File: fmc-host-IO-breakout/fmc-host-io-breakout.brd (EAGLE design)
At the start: 135 x 195 mm, 79 parts, among them J4 12226-8250-00FR, X1 1503_02

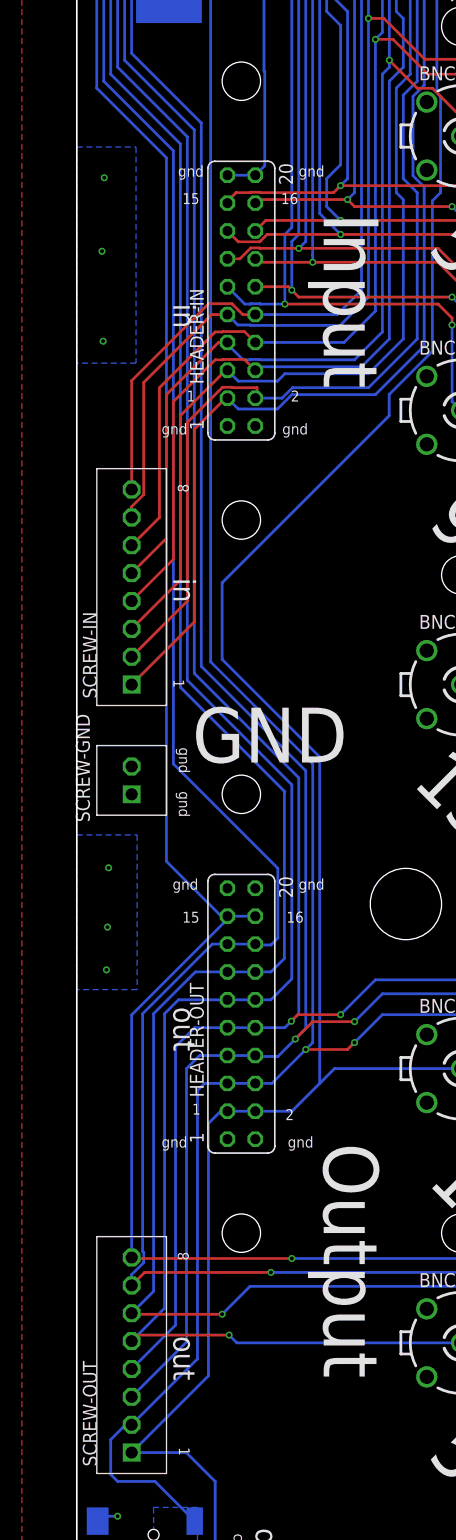
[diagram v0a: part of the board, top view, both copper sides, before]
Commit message: Made analog io board compatible with screwless screw terminals
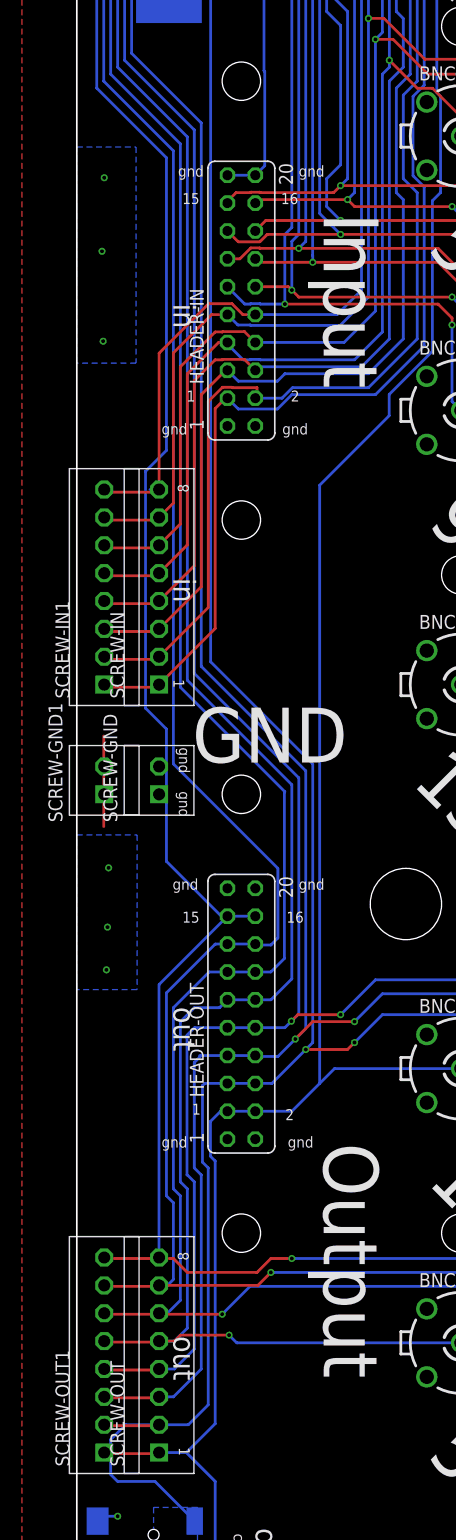
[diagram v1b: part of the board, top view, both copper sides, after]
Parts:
- added SCREW-GND1: SCREW2, jonnew:SCREW2
- added SCREW-IN1, SCREW-OUT1: SCREW8, jonnew:SCREW8
- moved SCREW-GND 2.50 mm to (-37.5, -25.0)
- moved SCREW-IN 2.50 mm to (-37.5, -15.0)
- moved SCREW-OUT 2.50 mm to (-37.5, -85.0)
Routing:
- net AOUT0: track 244.6 -> 233.1 mm
- net AGND: track 229.1 -> 237.3 mm
- net S$9: track 0.00 -> 5.08 mm
- net S$8: track 0.00 -> 5.08 mm
- net S$7: track 0.00 -> 5.08 mm
- net S$6: track 0.00 -> 5.08 mm
- net S$5: track 0.00 -> 5.08 mm
- net S$4: track 0.00 -> 5.08 mm
- net S$3: track 0.00 -> 5.08 mm
- net S$2: track 0.00 -> 5.08 mm
- net S$16: track 0.00 -> 5.08 mm
- net S$15: track 0.00 -> 5.08 mm
- net S$14: track 0.00 -> 5.08 mm
- net S$13: track 0.00 -> 5.08 mm
- net S$12: track 0.00 -> 5.08 mm
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
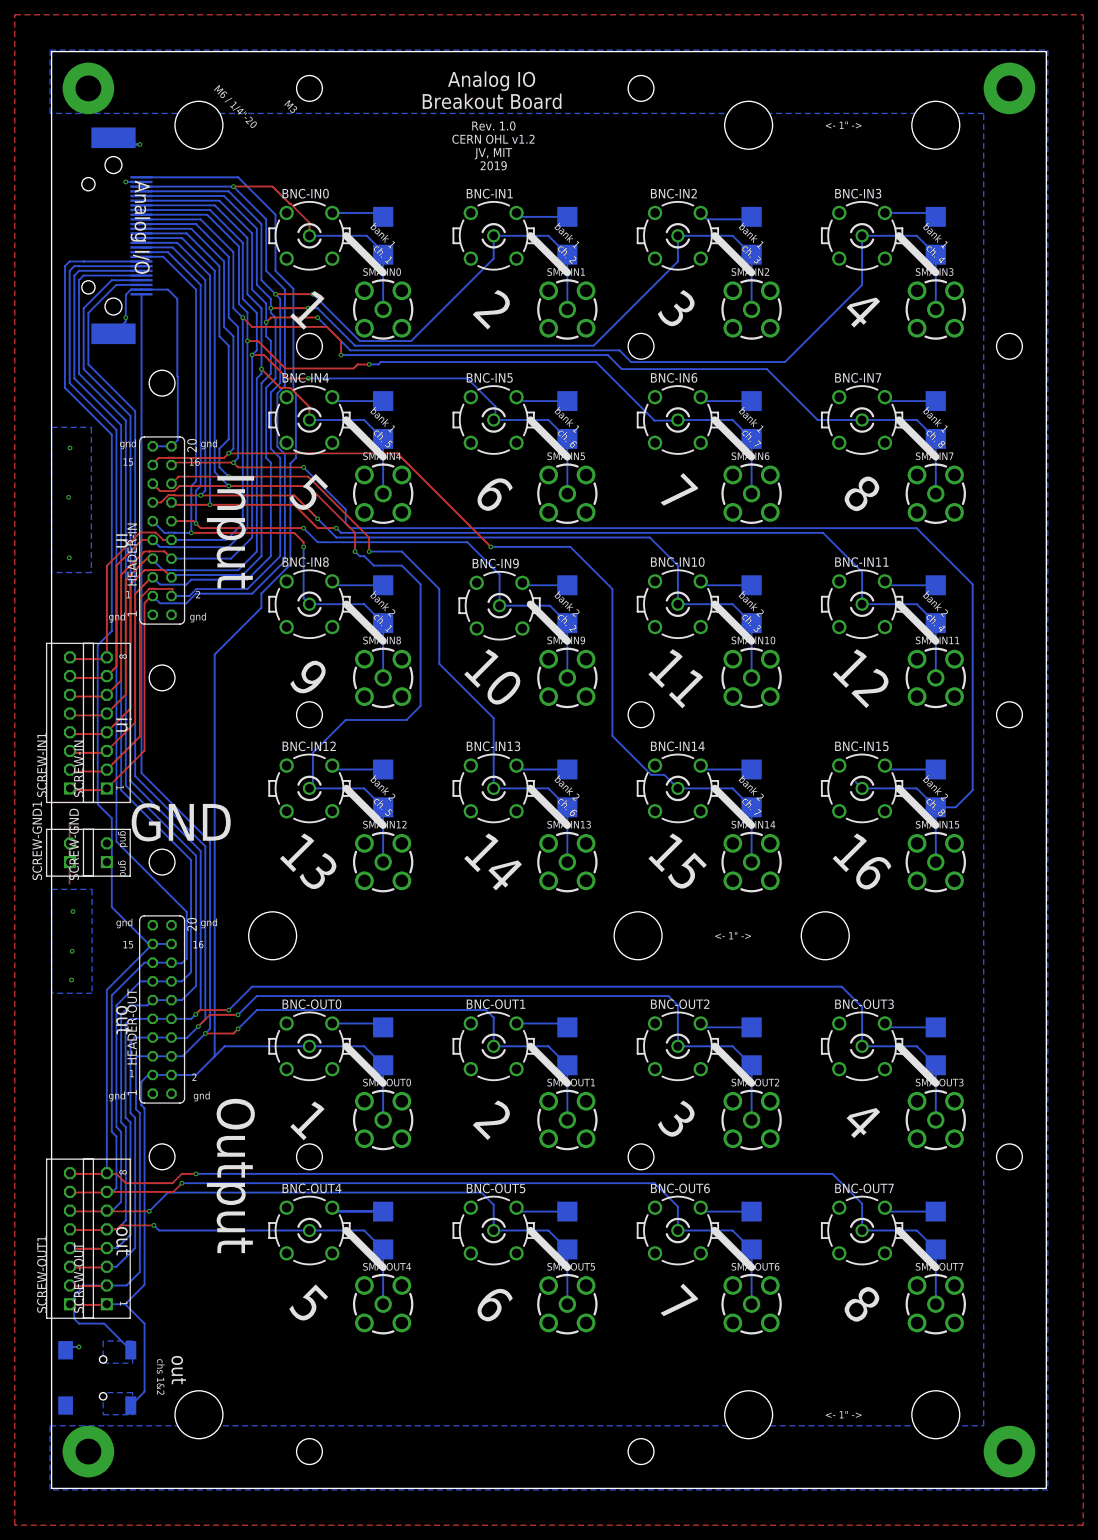
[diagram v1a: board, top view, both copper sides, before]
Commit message: Connected screw terminal rows in analog io board
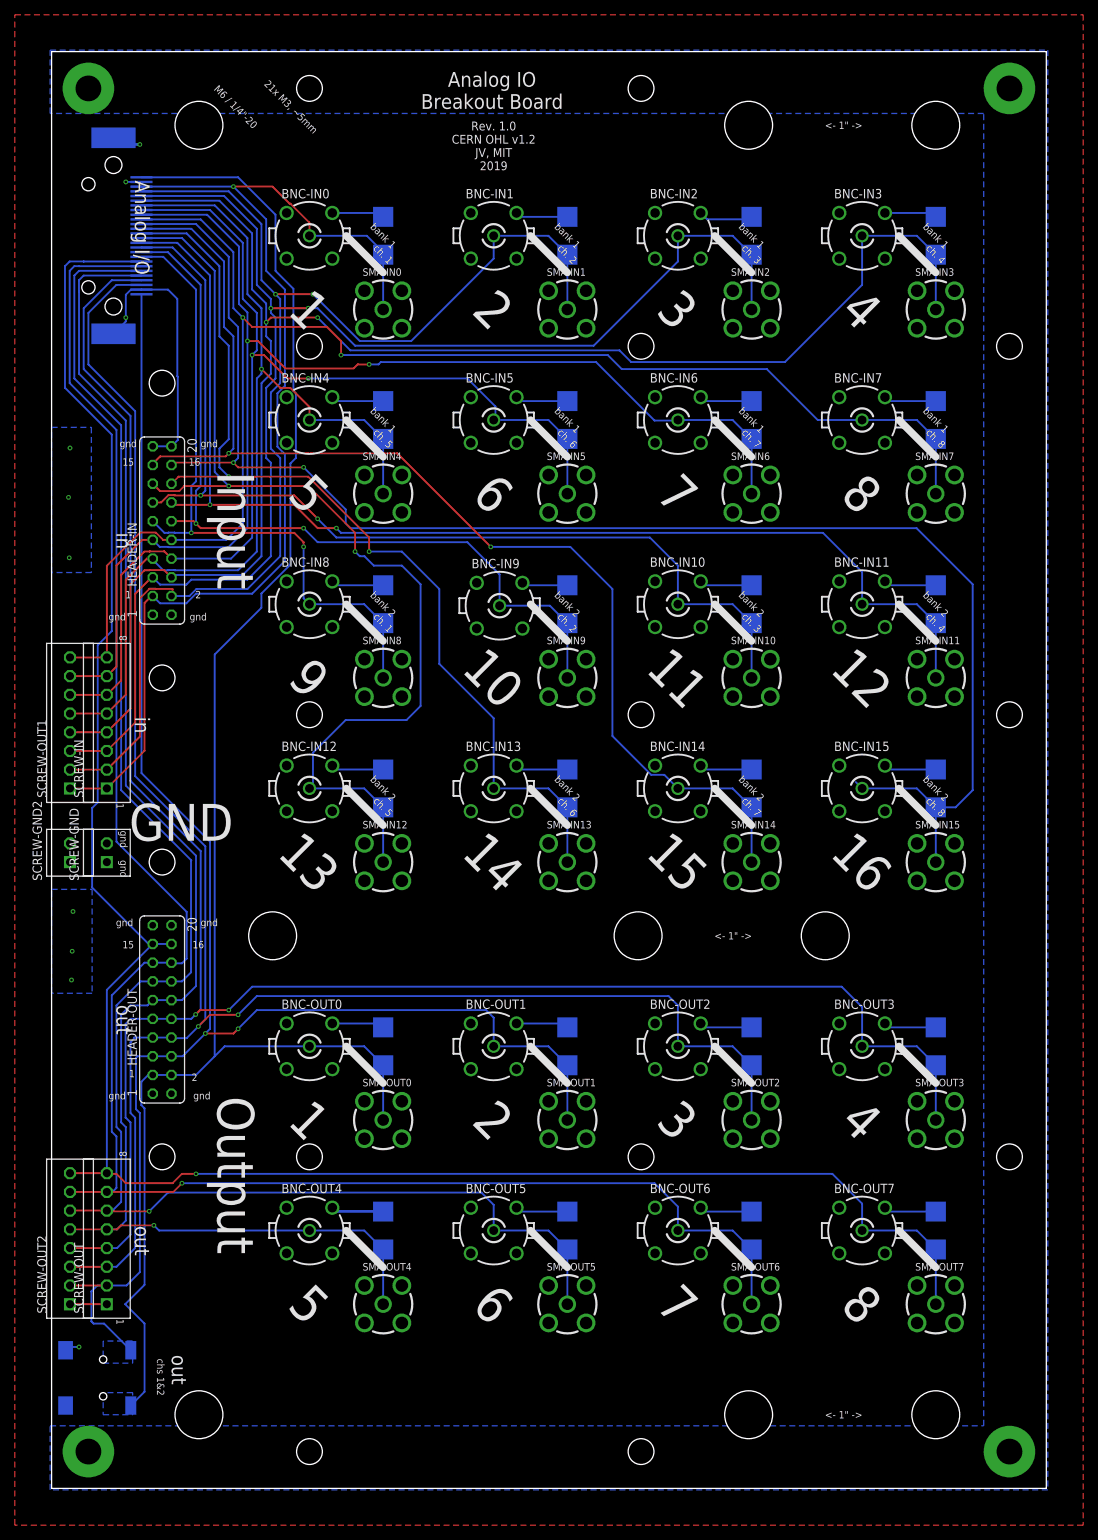
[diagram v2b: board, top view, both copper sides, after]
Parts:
- removed SCREW-IN1: SCREW8, jonnew:SCREW8
- added SCREW-OUT2: SCREW8, jonnew:SCREW8
- moved SCREW-OUT1 70.0 mm to (-42.5, -15.0)
- renumbered SCREW-GND1 to SCREW-GND2
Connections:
- net AGND: now also SCREW-GND2.P$1, SCREW-GND2.P$2
- net AIN0: now also SCREW-OUT1.1
- net AIN1: now also SCREW-OUT1.2
- net AIN2: now also SCREW-OUT1.3
- net AIN3: now also SCREW-OUT1.4
- net AIN4: now also SCREW-OUT1.5
- net AIN5: now also SCREW-OUT1.6
- net AIN6: now also SCREW-OUT1.7
- net AIN7: now also SCREW-OUT1.8
- net AOUT0: now also SCREW-OUT2.1
- net AOUT1: now also SCREW-OUT2.2
- net AOUT2: now also SCREW-OUT2.3
- net AOUT3: now also SCREW-OUT2.4
- net AOUT4: now also SCREW-OUT2.5
- net AOUT5: now also SCREW-OUT2.6
- net AOUT6: now also SCREW-OUT2.7
- net AOUT7: now also SCREW-OUT2.8
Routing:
- net AGND: track 237.3 -> 229.1 mm
- net AOUT7: track 273.7 -> 279.4 mm
- net S$9: track 5.08 -> 0.00 mm
- net S$8: track 5.08 -> 0.00 mm
- net S$7: track 5.08 -> 0.00 mm
- net S$6: track 5.08 -> 0.00 mm
- net S$5: track 5.08 -> 0.00 mm
- net S$4: track 5.08 -> 0.00 mm
- net S$3: track 5.08 -> 0.00 mm
- net S$2: track 5.08 -> 0.00 mm
- net S$16: track 5.08 -> 0.00 mm
- net S$15: track 5.08 -> 0.00 mm
- net S$14: track 5.08 -> 0.00 mm
- net S$13: track 5.08 -> 0.00 mm
- net S$12: track 5.08 -> 0.00 mm
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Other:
- board text added: "21x M3, ~5mm"
- board text removed: "M3"
